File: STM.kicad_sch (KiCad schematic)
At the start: 0 parts

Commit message: added stm pins
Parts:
- added D1: (no value), symbol Diode:1N914
- added J2: CONN HEADER SMD 10POS 1.27MM, footprints:CNC_3221-10-0300-00, symbol symbols:3221-10-0300-00
- added R5, R7, R8, R9: 100, symbol Device:R_Small_US
- added TP1, TP2, TP3, TP4: TestPoint, symbol Connector:TestPoint
- added U1: STM32C542CCU6, footprints:UFQFPN-48_STM, symbol symbols:STM32C542CCU6
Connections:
- new net: D1.2 (A), J2.1
- new net 3V3: D1.1 (K)
- new net GND: J2.3, J2.5
- new net NRST: J2.10, U1.7 (NRST)
- new net PA1/ERRQ_ext: U1.11 (PA1)
- new net PA2/ERRQ_res: U1.12 (PA2)
- new net PA3/NSLEEP: U1.13 (PA3)
- new net PA4/ERR_ext_out: U1.14 (PA4)
- new net PA5/ERR_loc_OUT: U1.15 (PA5)
- new net PA6/ERRQ: U1.16 (PA6)
- new net PA8/STBY: U1.29 (PA8)
- new net PB5/FDCAN2_RX: U1.41 (PB5)
- new net PB6/FDCAN2_TX: U1.42 (PB6)
- new net PB8/UART4_RX: R9.2, TP4.1, U1.45 (PB8)
- new net PB9/UART4_TX: R8.2, TP3.1, U1.46 (PB9)
- new net SWCLK: J2.4, R7.1
- new net SWCLK/PA14: R7.2, TP2.1, U1.37 (PA14)
- new net SWDIO: J2.2, R5.1
- new net SWDIO/PA13: R5.2, TP1.1, U1.34 (PA13)
- new net USART4_RX: J2.8, R9.1
- new net USART4_TX: J2.6, R8.1
- no-connect marks 0 -> 2
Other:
- note added: "STLink"
- note added: "TPs and Termination for STLink"
- note added: "fix diode, its the same one that midsun uses for stlink"
- note added: "remmeber to add test points to bms afe"

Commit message: finished can and power
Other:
- moved on the sheet: D1, J2, R5, R7, R8, R9, TP1, TP2, TP3, TP4

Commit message: schematic done
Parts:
- removed D1: (no value), symbol Diode:1N914
- added C14: 2.2uF, symbol Device:C_Small
- added C15, C16, C17, C18, C19, C20: 10uF, symbol Device:C_Small
- added C21: 100nF, symbol Device:C_Small
- added D3: DIODE SCHOTTKY 30V 1A SOD323F, footprints:P39_SOD-323P, symbol symbols:SDB13HS-AQ
- added FB1: FERRITE BEAD 600 OHM 0603 1LN, Resistor_SMD:R_0603_1608Metric, symbol Device:FerriteBead_Small
- added R13: 10K, symbol Device:R_Small_US
- added R14: 1K, symbol Device:R_Small_US
- added TP5, TP6: TestPoint, symbol Connector:TestPoint
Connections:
- net 3V3: now also U1.24 (VDD), U1.36 (VDD), U1.48 (VDD), C15.1, C16.1, C17.1, C18.1, D3.1 (K), FB1.1, R13.1
- net GND: now also U1.23 (VSS), U1.35 (VSS), U1.47 (VSS), U1.49 (VSS), U1.8 (VREF-), C14.2, C15.2, C16.2, C17.2, C18.2, C19.2, C20.2, C21.2, R14.2
- net NRST: now also TP5.1
- net PB0/ADC1_IN6: now reaches U1.18 (PB0)
- net at U1.44 (PH2-BOOT0): now also R14.1, TP6.1
- net at J2.1: now also D3.2 (A)
- net at U1.22 (VCAP): now also C14.1
- net at U1.9 (VREF+): now also C19.1, C20.1, FB1.2
- new net: C21.1, R13.2
- no-connect marks 2 -> 25
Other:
- note removed: "fix diode, its the same one that midsun uses for stlink"
- moved on the sheet: J2, R5, R7, R8, R9, TP1, TP2, TP3, TP4, U1A, U1B

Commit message: damir review
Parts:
- removed C20: 10uF, symbol Device:C_Small
- C15: value 10uF -> 4.7uF
- C16, C17, C18, C19: value 10uF -> 100nF
- TP1, TP2, TP3, TP4: footprint (none) -> TestPoint:TestPoint_Pad_D1.0mm
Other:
- moved on the sheet: C15, C19, FB1

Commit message: changed stm and stlink
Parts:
- removed C14: 2.2uF, symbol Device:C_Small
- removed J2: CONN HEADER SMD 10POS 1.27MM, footprints:CNC_3221-10-0300-00, symbol symbols:3221-10-0300-00
- removed U1: STM32C542CCU6, footprints:UFQFPN-48_STM, symbol symbols:STM32C542CCU6
- added C20: 10nF, symbol Device:C_Small
- added J7: PIN HEADER 2.54MM PITCH STR DIP, footprints:CONN6x1_G800W302018EU_AMP, symbol symbols:G800W302018EU
- added R21: 100, symbol Device:R_Small_US
- added TP7: TestPoint, TestPoint:TestPoint_Pad_D1.0mm, symbol Connector:TestPoint
- added U5: STM32L431KBU6TR, footprints:UFQFPN-32, symbol symbols:STM32L431KBU6TR
- C18: value 100nF -> 1uF
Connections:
- net 3V3: now also U5.1 (VDD), U5.17 (VDD); no longer C18.1
- net GND: now also C20.2, J7.3, U5.16 (VSS), U5.32 (VSS)
- net NRST: now also J7.5, U5.4 (NRST)
- net PA1/ERRQ_ext: now also U5.7 (PA1)
- net PA2/ERRQ_res: now also U5.8 (PA2)
- net PA3/NSLEEP: now also U5.9 (PA3)
- net PA4/ERR_ext_out: now also U5.10 (PA4)
- net PA5/ERR_loc_OUT: now also U5.11 (PA5)
- net PA6/ERRQ: now also U5.12 (PA6)
- net PB0/ADC1_IN6: now also U5.6 (PA0/CK_IN)
- net PB9/UART4_TX: now also U5.19 (PA9)
- net SWCLK: now also J7.2
- net SWCLK/PA14: now also U5.24 (PA14)
- net SWDIO: now also J7.4
- net SWDIO/PA13: now also U5.23 (PA13)
- net PH3/BOOT0: now reaches R14.1, TP6.1
- net PH3/BOOT0: now also U5.31 (PH3/BOOT0)
- net at D3.2 (A): now also J7.1
- net at C19.1, FB1.2: now also C18.1, C20.1, U5.5 (VDDA/VREF+)
- new net PA7/STBY: U5.13 (PA7)
- new net PB10/UART4_RX: U5.20 (PA10)
- new net PB11/FDCAN2_RX: U5.21 (PA11)
- new net PB12/FDCAN2_TX: U5.22 (PA12)
- new net SWO: J7.6, R21.1
- new net SWO/PB3: R21.2, TP7.1, U5.26 (PB3)
- no-connect marks 25 -> 10
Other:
- moved on the sheet: R5, R7, R8, R9, TP1, TP2, TP3, TP4

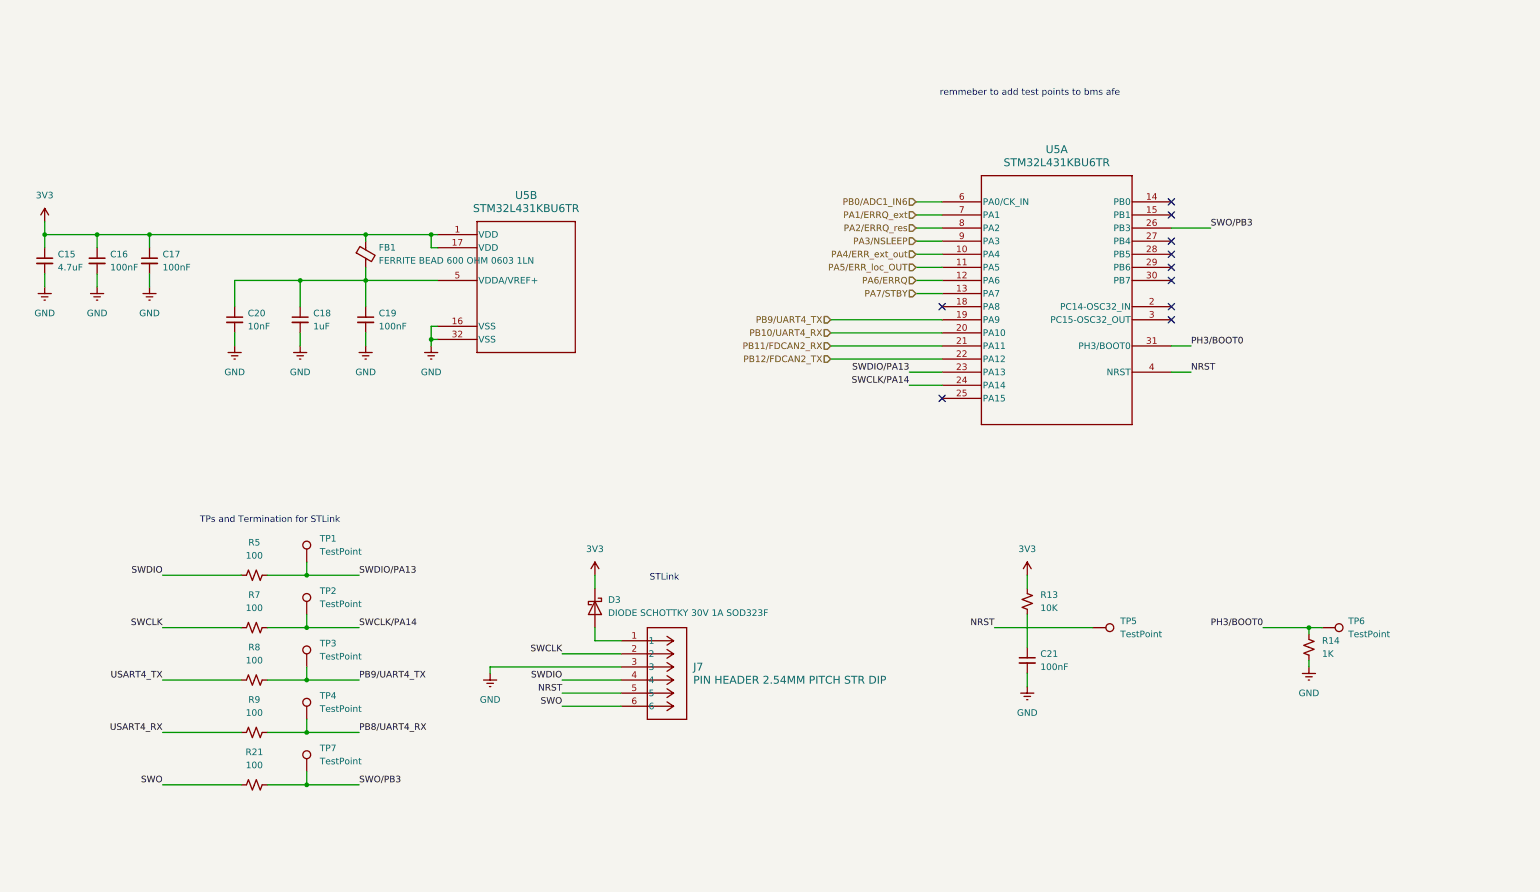
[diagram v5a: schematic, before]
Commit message: fixed csense connectors and stm
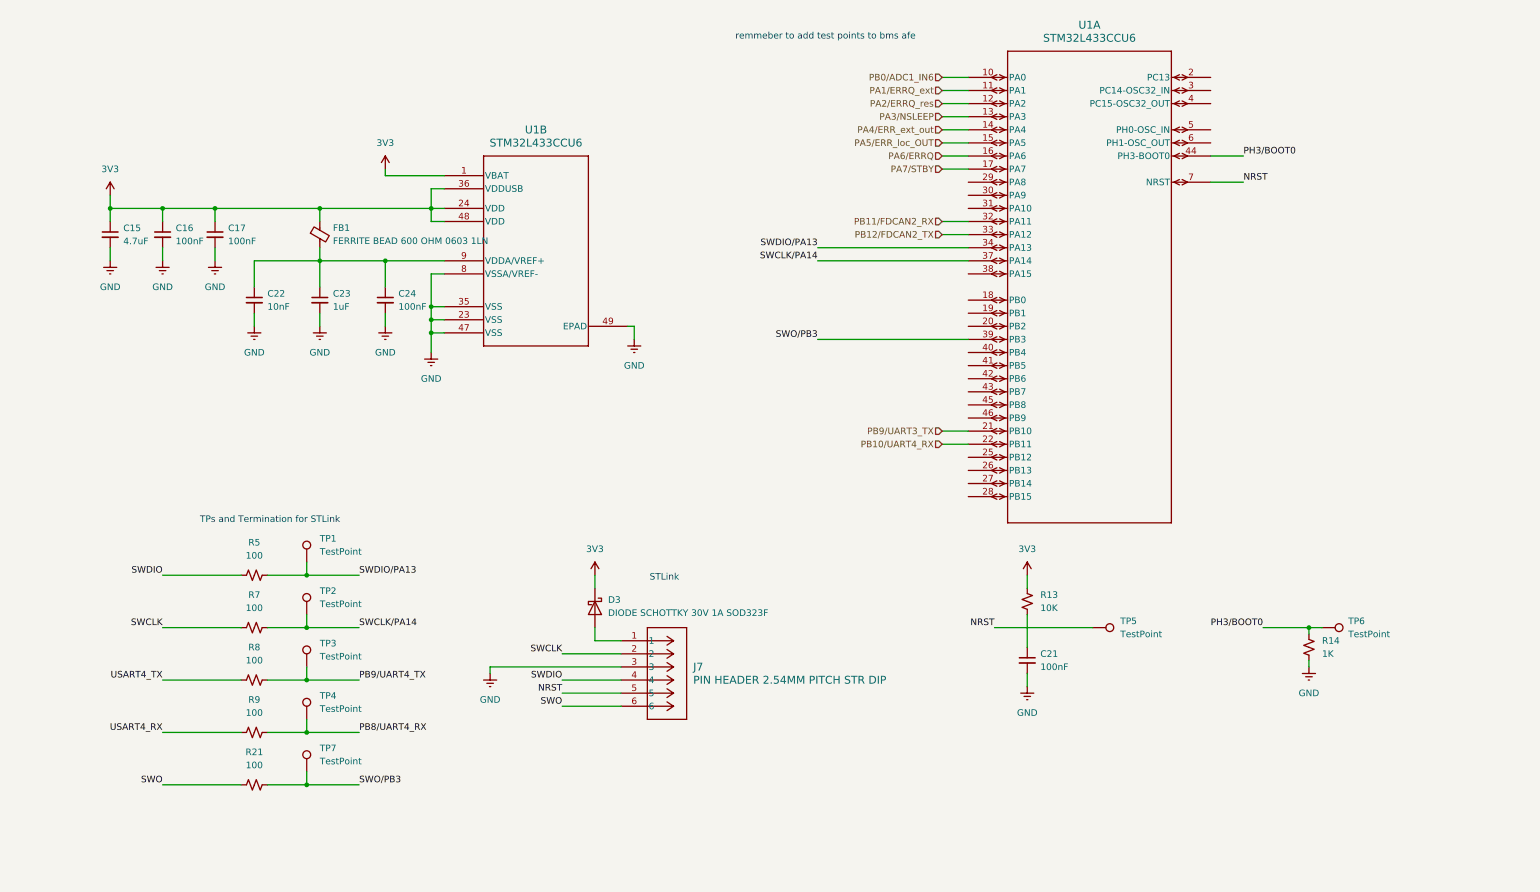
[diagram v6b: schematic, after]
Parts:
- removed C18: 1uF, symbol Device:C_Small
- removed C19: 100nF, symbol Device:C_Small
- removed C20: 10nF, symbol Device:C_Small
- removed U5: STM32L431KBU6TR, footprints:UFQFPN-32, symbol symbols:STM32L431KBU6TR
- added C22: 10nF, symbol Device:C_Small
- added C23: 1uF, symbol Device:C_Small
- added C24: 100nF, symbol Device:C_Small
- added U1: STM32L433CCU6, footprints:UFQFPN48-7x7mm, symbol symbols:STM32L433CCU6
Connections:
- net 3V3: now also U1.1 (VBAT), U1.24 (VDD), U1.36 (VDDUSB), U1.48 (VDD)
- net GND: now also C22.2, C23.2, C24.2, U1.23 (VSS), U1.35 (VSS), U1.47 (VSS), U1.49 (EPAD), U1.8 (VSSA/VREF-)
- net NRST: now also U1.7 (NRST)
- net PA1/ERRQ_ext: now also U1.11 (PA1)
- net PA2/ERRQ_res: now also U1.12 (PA2)
- net PA3/NSLEEP: now also U1.13 (PA3)
- net PA4/ERR_ext_out: now also U1.14 (PA4)
- net PA5/ERR_loc_OUT: now also U1.15 (PA5)
- net PA6/ERRQ: now also U1.16 (PA6)
- net PA7/STBY: now also U1.17 (PA7)
- net PB0/ADC1_IN6: now also U1.10 (PA0)
- net PB10/UART4_RX: now also U1.22 (PB11)
- net PB11/FDCAN2_RX: now also U1.32 (PA11)
- net PB12/FDCAN2_TX: now also U1.33 (PA12)
- net PH3/BOOT0: now also U1.44 (PH3-BOOT0)
- net SWCLK/PA14: now also U1.37 (PA14)
- net SWDIO/PA13: now also U1.34 (PA13)
- net SWO/PB3: now also U1.39 (PB3)
- net at FB1.2: now also C22.1, C23.1, C24.1, U1.9 (VDDA/VREF+)
- new net PB9/UART3_TX: U1.21 (PB10)
- no-connect marks 10 -> 0

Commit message: tweaked a little
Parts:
- added C25, C26: 10pF, symbol Device:C_Small
- added R22: 330, symbol Device:R_Small_US
- added X1: CRYSTAL 32.0000MHZ 10PF SMD, footprints:SMD4_RH100_2P5X3P2-2P2_RAL, symbol symbols:RH100-32.000-10-F-2020-EXT-TR
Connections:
- net GND: now also C25.2, C26.2
- net PH0-OSC_IN: now reaches U1.5 (PH0-OSC_IN)
- net PH0-OSC_IN: now also C25.1, X1.1
- net PH1-OSC_OUT: now reaches U1.6 (PH1-OSC_OUT)
- net PH1-OSC_OUT: now also R22.1
- net PB0/ADC1_IN6 renamed PA/ADC1_IN5
- net PB10/UART4_RX renamed PB11/UART4_RX
- net PB11/FDCAN2_RX renamed PB11/CAN1_RX
- net PB12/FDCAN2_TX renamed PB12/CAN1_TX
- net PB9/UART3_TX renamed PB10/UART3_TX
- new net: C26.1, R22.2, X1.3
- no-connect marks 0 -> 2
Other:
- moved on the sheet: C15, C16, C17, C22, C23, C24, D3, FB1, J7, R21, R5, R7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

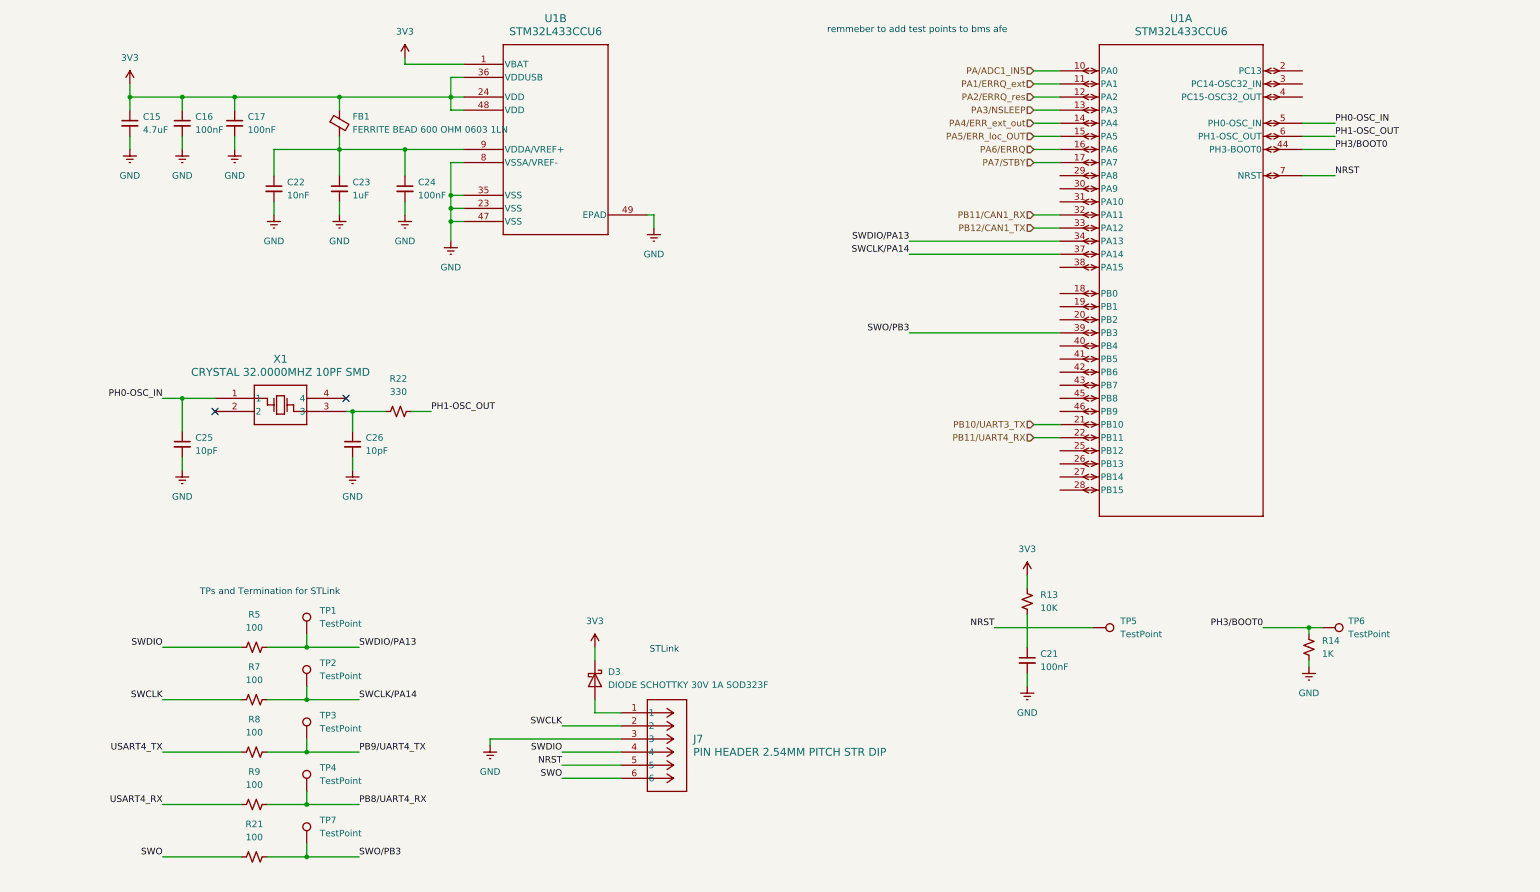
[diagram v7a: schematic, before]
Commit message: added passives
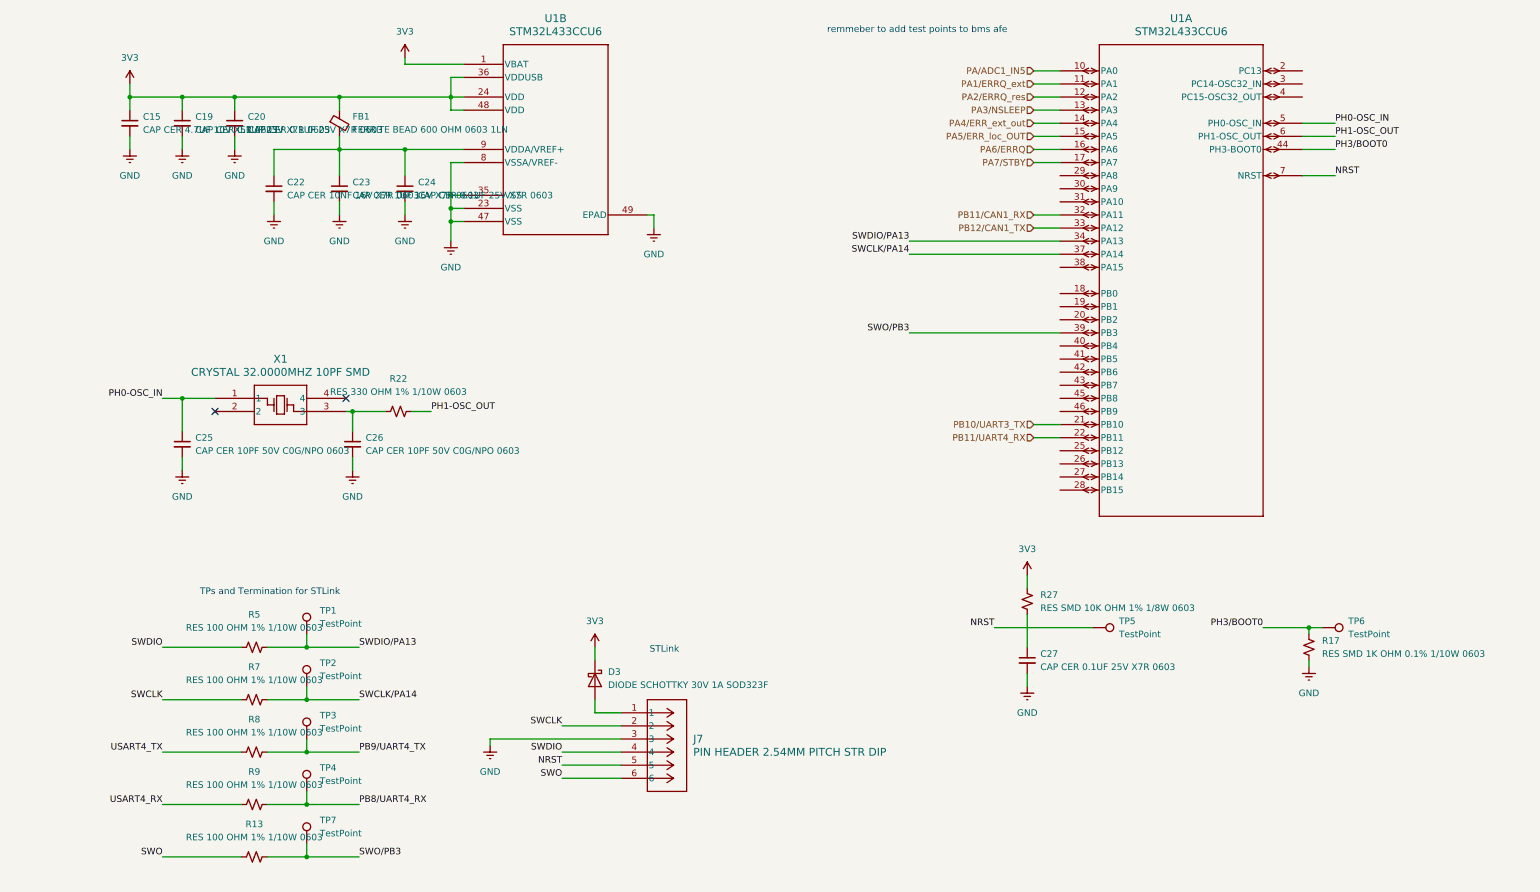
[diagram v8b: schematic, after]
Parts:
- removed C16, C17, C21: 100nF, symbol Device:C_Small
- removed R14: 1K, symbol Device:R_Small_US
- removed R21: 100, symbol Device:R_Small_US
- added C19, C20, C27: CAP CER 0.1UF 25V X7R 0603, Capacitor_SMD:C_0603_1608Metric, symbol Device:C_Small
- added R17: RES SMD 1K OHM 0.1% 1/10W 0603, Resistor_SMD:R_0603_1608Metric, symbol Device:R_Small_US
- added R27: RES SMD 10K OHM 1% 1/8W 0603, Resistor_SMD:R_0603_1608Metric, symbol Device:R_Small_US
- C15: value 4.7uF -> CAP CER 4.7UF 10V X5R 0603; footprint (none) -> Capacitor_SMD:C_0603_1608Metric
- C22: value 10nF -> CAP CER 10NF 16V X7R 0603; footprint (none) -> Capacitor_SMD:C_0603_1608Metric
- C23: value 1uF -> CAP CER 1UF 16V X7R 0603; footprint (none) -> Capacitor_SMD:C_0603_1608Metric
- C24: value 100nF -> CAP CER 0.1UF 25V X7R 0603; footprint (none) -> Capacitor_SMD:C_0603_1608Metric
- C25, C26: value 10pF -> CAP CER 10PF 50V C0G/NPO 0603; footprint (none) -> Capacitor_SMD:C_0603_1608Metric
- R13: value 10K -> RES 100 OHM 1% 1/10W 0603; footprint (none) -> Resistor_SMD:R_0603_1608Metric
- R22: value 330 -> RES 330 OHM 1% 1/10W 0603; footprint (none) -> Resistor_SMD:R_0603_1608Metric
- R5, R7, R8, R9: value 100 -> RES 100 OHM 1% 1/10W 0603; footprint (none) -> Resistor_SMD:R_0603_1608Metric
- TP5, TP6: footprint (none) -> TestPoint:TestPoint_Pad_D1.0mm
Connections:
- net 3V3: now also C19.1, C20.1, R27.1; no longer R13.1
- net GND: now also C19.2, C20.2, C27.2, R17.1
- net PH3/BOOT0: now also R17.2
- net SWO: now also R13.1
- net SWO/PB3: now also R13.2
- new net: C27.1, R27.2
